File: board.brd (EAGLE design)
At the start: 26.3 x 33.6 mm, 46 parts, among them IC1 ATMEGA48/88/168-AU, IC2 TP4056, IC3 MAX31865, Q1 PH2925U, Q2 IRLML2244, U1 LM3480-3.3

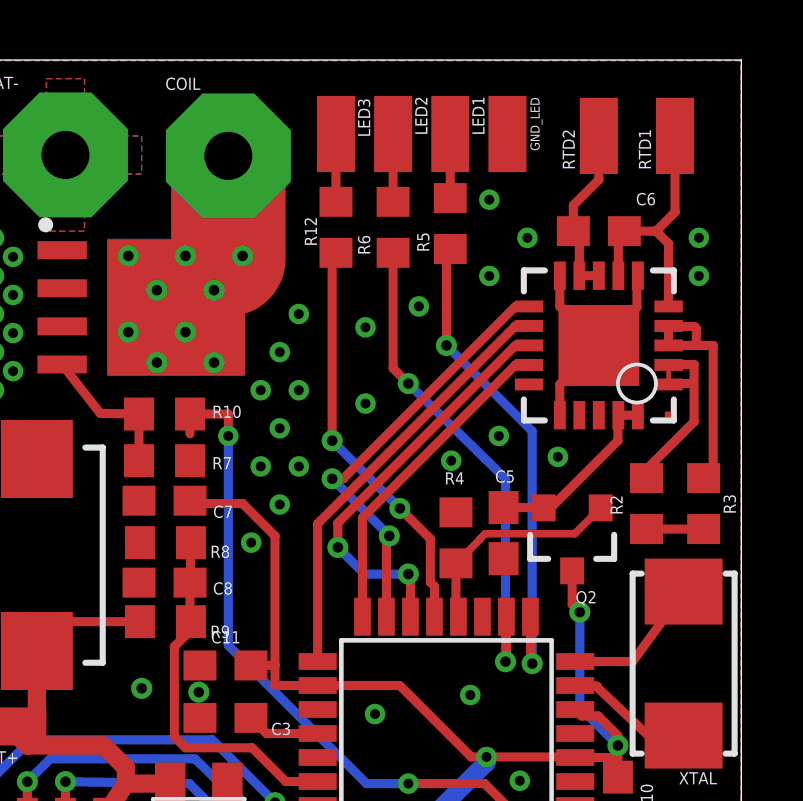
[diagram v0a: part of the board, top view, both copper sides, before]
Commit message: adding tstop for charger heat transfer
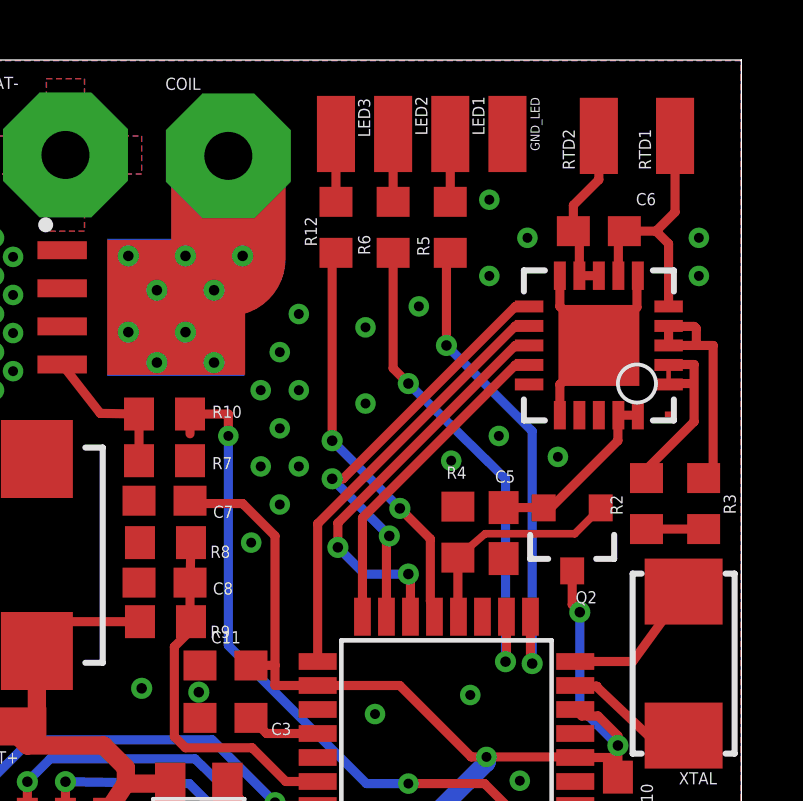
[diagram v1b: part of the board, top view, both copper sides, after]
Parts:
- moved R4 0.20 mm to (16.9, 17.9)
- moved R5 0.13 mm to (16.6, 28.1)
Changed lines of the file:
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@@
 <text x="25.4" y="0.635" size="1.6764" layer="22" rot="MR0">Vapoduino_v0.2</text>
 <rectangle x1="5.207" y1="23.114" x2="9.779" y2="27.686" layer="16"/>
+<rectangle x1="1.4605" y1="4.445" x2="4.8895" y2="6.858" layer="29"/>
 </plain>
 <attributes>
@@
 <attribute name="VALUE" x="23.1775" y="19.4945" size="1.27" layer="27" rot="R270"/>
 </element>
-<element name="R5" library="rcl" package="R0603" value="1K" x="16.637" y="28.194" smashed="yes" rot="R270">
-<attribute name="NAME" x="15.9385" y="27.2415" size="0.4064" layer="25" rot="R90"/>
-<attribute name="VALUE" x="14.732" y="28.829" size="1.27" layer="27" rot="R270"/>
+<element name="R5" library="rcl" package="R0603" value="1K" x="16.637" y="28.067" smashed="yes" rot="R270">
+<attribute name="NAME" x="15.9385" y="27.1145" size="0.4064" layer="25" rot="R90"/>
+<attribute name="VALUE" x="14.732" y="28.702" size="1.27" layer="27" rot="R270"/>
 </element>
 <element name="R6" library="rcl" package="R0603" value="1K" x="14.732" y="28.067" smashed="yes" rot="R270">
@@
 <attribute name="VALUE" x="21.717" y="17.907" size="0.4064" layer="27" rot="R180"/>
 </element>
-<element name="R4" library="rcl" package="R0603" value="10k" x="16.8275" y="17.7165" smashed="yes" rot="R90">
-<attribute name="NAME" x="16.4465" y="19.4945" size="0.4064" layer="25"/>
-<attribute name="VALUE" x="18.7325" y="17.0815" size="1.27" layer="27" rot="R90"/>
+<element name="R4" library="rcl" package="R0603" value="10k" x="16.891" y="17.907" smashed="yes" rot="R90">
+<attribute name="NAME" x="16.51" y="19.685" size="0.4064" layer="25"/>
+<attribute name="VALUE" x="18.796" y="17.272" size="1.27" layer="27" rot="R90"/>
 </element>
 <element name="R10" library="rcl" package="R0603" value="100" x="7.112" y="21.844" smashed="yes">
@@
 <contactref element="Q2" pad="1"/>
 <contactref element="R4" pad="1"/>
-<wire x1="16.91" y1="15.0876" x2="16.8275" y2="15.0876" width="0.3048" layer="1"/>
-<wire x1="16.8275" y1="15.0876" x2="16.8275" y2="16.8665" width="0.3048" layer="1"/>
-<wire x1="16.8275" y1="16.8665" x2="17.6356" y2="17.6746" width="0.254" layer="1"/>
-<wire x1="17.6356" y1="17.6746" x2="17.6356" y2="17.69098125" width="0.254" layer="1"/>
+<wire x1="16.91" y1="15.0876" x2="16.891" y2="15.0876" width="0.3048" layer="1"/>
+<wire x1="16.891" y1="15.0876" x2="16.891" y2="17.057" width="0.3048" layer="1"/>
 <wire x1="20.78915" y1="17.85465" x2="21.651" y2="18.7165" width="0.254" layer="1"/>
 <wire x1="17.79926875" y1="17.85465" x2="20.78915" y2="17.85465" width="0.254" layer="1"/>
-<wire x1="17.6356" y1="17.69098125" x2="17.79926875" y2="17.85465" width="0.254" layer="1"/>
+<wire x1="16.8736" y1="17.05598125" x2="17.79926875" y2="17.85465" width="0.254" layer="1"/>
+<wire x1="16.891" y1="17.057" x2="16.8736" y2="17.05598125" width="0" layer="19" extent="1-1"/>
 </signal>
 <signal name="D9_LED3">
 <contactref element="IC1" pad="13"/>
 <contactref element="R12" pad="2"/>
-<wire x1="16.11" y1="15.0876" x2="16.11" y2="16.10295" width="0.3048" layer="1"/>
-<wire x1="16.11" y1="16.10295" x2="15.9727" y2="16.24025" width="0.3048" layer="1"/>
-<wire x1="15.9727" y1="16.24025" x2="15.9727" y2="17.6823" width="0.3048" layer="1"/>
+<wire x1="16.11" y1="15.0876" x2="15.983" y2="15.59495" width="0.3048" layer="1"/>
+<wire x1="15.983" y1="15.59495" x2="15.9727" y2="15.60525" width="0.3048" layer="1"/>
+<wire x1="15.9727" y1="15.60525" x2="15.9727" y2="17.6823" width="0.3048" layer="1"/>
 <via x="14.95696875" y="18.69803125" extent="1-16" drill="0.35"/>
 <wire x1="14.95696875" y1="18.69803125" x2="12.7" y2="20.955" width="0.3048" layer="16"/>
@@
 <via x="16.51" y="24.13" extent="1-16" drill="0.35"/>
 <wire x1="16.51" y1="24.13" x2="16.51" y2="27.217" width="0.3048" layer="1"/>
-<wire x1="16.51" y1="27.217" x2="16.637" y2="27.344" width="0.3048" layer="1"/>
+<wire x1="16.51" y1="27.217" x2="16.637" y2="27.217" width="0.3048" layer="1"/>
 </signal>
 <signal name="VBAT">
@@
 <contactref element="R5" pad="1"/>
 <contactref element="LED1" pad="1"/>
-<wire x1="16.637" y1="31.1785" x2="16.637" y2="29.044" width="0.3048" layer="1"/>
+<wire x1="16.637" y1="31.1785" x2="16.637" y2="28.917" width="0.3048" layer="1"/>
 </signal>
 <signal name="COIL">

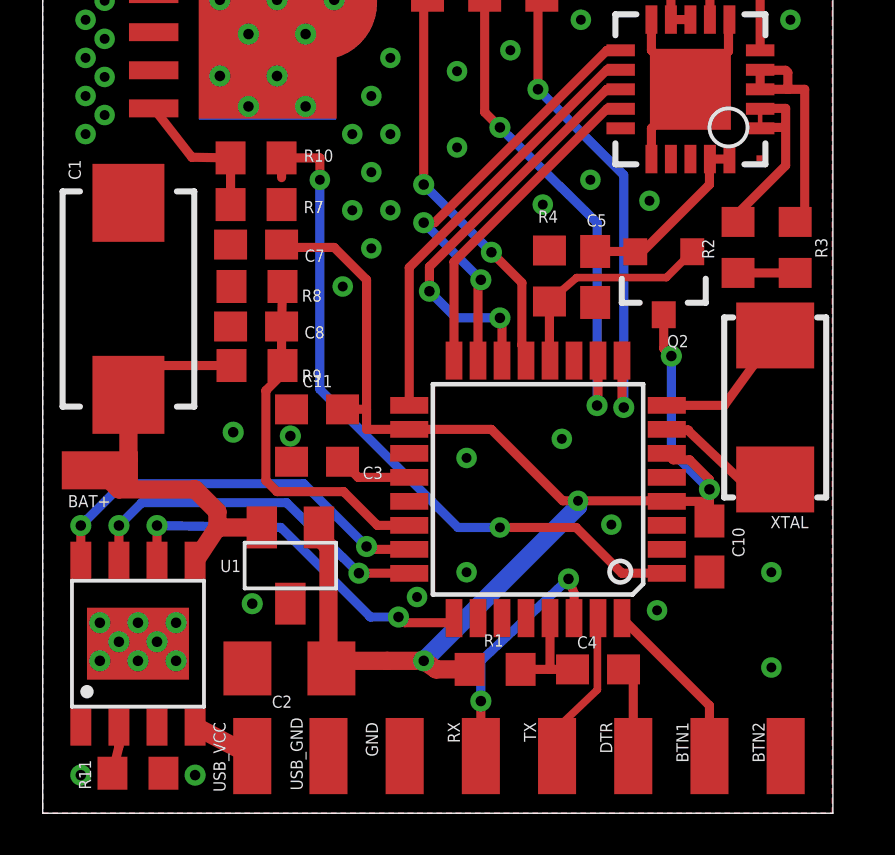
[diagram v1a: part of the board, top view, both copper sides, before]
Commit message: using MCP1703 as vreg
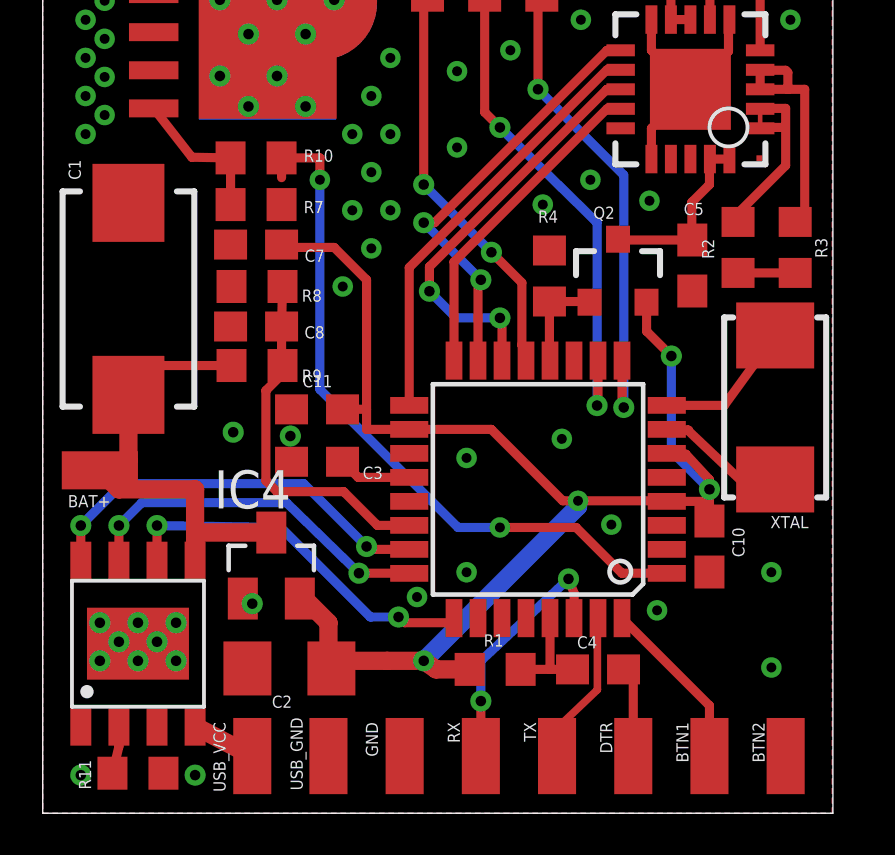
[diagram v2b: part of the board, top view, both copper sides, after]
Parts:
- removed U1: LM3480-3.3, regulators:SOT-23-3
- added IC4: MCP1703CB, linear:SOT23
- moved C5 3.26 mm to (21.7, 18.3)
- moved Q2 1.56 mm to (19.2, 18.0), turned to 0 degrees
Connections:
- net GND: now also IC4.1; no longer U1.3
- net VBAT: now also IC4.3; no longer U1.2
- net VCC: now also IC4.2, Q2.2; no longer Q2.3, U1.1
- net VCC_MAX: now also Q2.3; no longer Q2.2
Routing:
- net D8_VCC_MAX: track 7.42 -> 3.33 mm
- net VCC: track 48.8 -> 47.5 mm
- net VBAT: track 14.9 -> 15.4 mm
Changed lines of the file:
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@@
 <attribute name="VALUE" x="19.78025" y="7.33425" size="1.27" layer="27" rot="R180"/>
 </element>
-<element name="C5" library="rcl" package="C0603" value="100n" x="18.415" y="17.87525" smashed="yes" rot="R270">
-<attribute name="NAME" x="18.12925" y="19.558" size="0.4064" layer="25"/>
-<attribute name="VALUE" x="15.875" y="19.14525" size="1.27" layer="27" rot="R270"/>
+<element name="C5" library="rcl" package="C0603" value="100n" x="21.6535" y="18.25625" smashed="yes" rot="R270">
+<attribute name="NAME" x="21.36775" y="19.939" size="0.4064" layer="25"/>
+<attribute name="VALUE" x="19.1135" y="19.52625" size="1.27" layer="27" rot="R270"/>
 </element>
 <element name="C6" library="rcl" package="C0603" value="100n" x="21.59" y="27.94" smashed="yes" rot="R180">
@@
 <attribute name="VALUE" x="8.509" y="11.557" size="1.27" layer="27"/>
 </element>
-<element name="Q2" library="SparkFun-DiscreteSemi" package="SOT23-3" value="IRLML2244" x="20.701" y="17.7165" smashed="yes" rot="R180">
-<attribute name="NAME" x="21.5265" y="15.9385" size="0.4064" layer="25" rot="R180"/>
-<attribute name="PROD_ID" value="TRANS-11153" x="20.701" y="17.7165" size="1.778" layer="27" rot="R180" display="off"/>
-<attribute name="VALUE" x="21.717" y="17.907" size="0.4064" layer="27" rot="R180"/>
+<element name="Q2" library="SparkFun-DiscreteSemi" package="SOT23-3" value="IRLML2244" x="19.177" y="18.034" smashed="yes">
+<attribute name="NAME" x="18.3515" y="19.812" size="0.4064" layer="25"/>
+<attribute name="PROD_ID" value="TRANS-11153" x="19.177" y="18.034" size="1.778" layer="27" display="off"/>
+<attribute name="VALUE" x="18.161" y="17.8435" size="0.4064" layer="27"/>
 </element>
 <element name="R4" library="rcl" package="R0603" value="10k" x="16.891" y="17.907" smashed="yes" rot="R90">
@@
 <attribute name="VALUE" x="12.827" y="31.1785" size="0.0254" layer="27"/>
 </element>
-<element name="U1" library="regulators" package="SOT-23-3" value="LM3480-3.3" x="8.255" y="8.255" smashed="yes" rot="R180">
-<attribute name="NAME" x="6.604" y="8.4455" size="0.4064" layer="21" ratio="12" rot="R180"/>
-</element>
+<element name="IC4" library="linear" library_urn="urn:adsk.eagle:library:262" package="SOT23" value="MCP1703CB" x="7.62" y="8.255"/>
 </elements>
 <signals>
@@
 <wire x1="22.225" y1="10.16" x2="22.225" y2="9.74" width="0.3048" layer="1"/>
 <wire x1="12.2174" y1="12.795" x2="14.9535125" y2="12.795" width="0.3048" layer="1"/>
-<contactref element="Q2" pad="3"/>
 <wire x1="20.7836" y1="10.414" x2="17.8435" y2="10.414" width="0.3048" layer="1"/>
 <wire x1="20.7836" y1="10.414" x2="20.8026" y2="10.395" width="0.3048" layer="1"/>
-<contactref element="U1" pad="1"/>
 <wire x1="9.62325" y1="4.826" x2="10.00425" y2="5.08" width="0.6096" layer="1"/>
 <wire x1="11.481821875" y1="5.08" x2="12.7" y2="5.08" width="0.6096" layer="1"/>
@@
 <wire x1="12.7" y1="5.08" x2="17.8435" y2="10.2235" width="0.6096" layer="16"/>
 <wire x1="17.8435" y1="10.2235" x2="17.8435" y2="10.414" width="0.6096" layer="16"/>
-<wire x1="9.2075" y1="9.525" x2="9.2075" y2="9.2075" width="0.6096" layer="1"/>
-<wire x1="9.2075" y1="9.2075" x2="9.525" y2="8.89" width="0.6096" layer="1"/>
-<wire x1="9.525" y1="8.89" x2="9.525" y2="4.92425" width="0.6096" layer="1"/>
+<wire x1="8.5725" y1="7.3025" x2="9.525" y2="6.35" width="0.6096" layer="1"/>
+<wire x1="9.525" y1="6.35" x2="9.525" y2="4.92425" width="0.6096" layer="1"/>
 <wire x1="9.525" y1="4.92425" x2="9.62325" y2="4.826" width="0.6096" layer="1"/>
 <wire x1="11.43725" y1="5.035428125" x2="11.481821875" y2="5.08" width="0.3048" layer="1"/>
 <wire x1="12.7" y1="5.08" x2="13.11275" y2="4.79425" width="0.6096" layer="1"/>
 <wire x1="13.11275" y1="4.79425" x2="14.23125" y2="4.79425" width="0.6096" layer="1"/>
-<wire x1="21.56385" y1="11.7792" x2="21.0184" y2="11.7792" width="0.3048" layer="1"/>
-<wire x1="21.0184" y1="11.7792" x2="20.8026" y2="11.995" width="0.3048" layer="1"/>
+<wire x1="21.43685" y1="11.9697" x2="20.8914" y2="11.9697" width="0.3048" layer="1"/>
+<wire x1="20.8914" y1="11.9697" x2="20.8026" y2="11.995" width="0.3048" layer="1"/>
 <wire x1="22.225" y1="9.74" x2="22.225" y2="10.795" width="0.3048" layer="1"/>
 <wire x1="22.225" y1="10.795" x2="22.225" y2="11.11805" width="0.3048" layer="1"/>
-<wire x1="22.225" y1="11.11805" x2="21.56385" y2="11.7792" width="0.3048" layer="1"/>
+<wire x1="22.225" y1="11.11805" x2="21.43685" y2="11.9697" width="0.3048" layer="1"/>
 <wire x1="17.8435" y1="10.414" x2="17.3345125" y2="10.414" width="0.3048" layer="1"/>
 <wire x1="17.3345125" y1="10.414" x2="14.9535125" y2="12.795" width="0.3048" layer="1"/>
@@
 <wire x1="22.225" y1="10.795" x2="20.955" y2="12.065" width="0.3048" layer="16"/>
 <wire x1="20.955" y1="12.065" x2="20.955" y2="15.24" width="0.3048" layer="16"/>
-<wire x1="20.701" y1="16.6165" x2="20.701" y2="15.494" width="0.3048" layer="1"/>
-<wire x1="20.701" y1="15.494" x2="20.955" y2="15.24" width="0.3048" layer="1"/>
+<wire x1="20.1295" y1="16.9545" x2="20.1295" y2="16.0655" width="0.3048" layer="1"/>
+<wire x1="20.1295" y1="16.0655" x2="20.955" y2="15.24" width="0.3048" layer="1"/>
 <via x="20.955" y="15.24" extent="1-16" drill="0.35"/>
 <wire x1="9.994" y1="13.462" x2="9.994" y2="13.466090625" width="0.3048" layer="1"/>
@@
 <wire x1="10.795" y1="13.466090625" x2="10.795" y2="12.795" width="0.3048" layer="1"/>
 <wire x1="10.795" y1="12.795" x2="12.2174" y2="12.795" width="0.3048" layer="1"/>
+<contactref element="Q2" pad="2"/>
+<contactref element="IC4" pad="2"/>
+<wire x1="20.1295" y1="16.9545" x2="20.127" y2="17.034" width="0" layer="19" extent="1-1"/>
+<wire x1="8.57" y1="7.155" x2="8.5725" y2="7.3025" width="0" layer="19" extent="1-1"/>
 </signal>
 <signal name="GND">
@@
 <vertex x="3.175" y="31.115"/>
 </polygon>
-<contactref element="U1" pad="3"/>
 <via x="8.255" y="12.573" extent="1-16" drill="0.35"/>
 <via x="6.985" y="6.985" extent="1-16" drill="0.35"/>
@@
 <via x="16.66875" y="20.28825" extent="1-16" drill="0.3302"/>
 <via x="20.22475" y="20.41525" extent="1-16" drill="0.3302"/>
+<contactref element="IC4" pad="1"/>
 </signal>
 <signal name="RXI">
@@
 <wire x1="16.91" y1="15.0876" x2="16.891" y2="15.0876" width="0.3048" layer="1"/>
 <wire x1="16.891" y1="15.0876" x2="16.891" y2="17.057" width="0.3048" layer="1"/>
-<wire x1="20.78915" y1="17.85465" x2="21.651" y2="18.7165" width="0.254" layer="1"/>
-<wire x1="17.79926875" y1="17.85465" x2="20.78915" y2="17.85465" width="0.254" layer="1"/>
-<wire x1="16.8736" y1="17.05598125" x2="17.79926875" y2="17.85465" width="0.254" layer="1"/>
-<wire x1="16.891" y1="17.057" x2="16.8736" y2="17.05598125" width="0" layer="19" extent="1-1"/>
+<wire x1="16.891" y1="17.057" x2="18.204" y2="17.057" width="0.3048" layer="1"/>
+<wire x1="18.204" y1="17.057" x2="18.227" y2="17.034" width="0.3048" layer="1"/>
 </signal>
 <signal name="D9_LED3">
@@
 <contactref element="C1" pad="+"/>
 <contactref element="BAT+" pad="1"/>
-<contactref element="U1" pad="2"/>
 <wire x1="2.8575" y1="11.7475" x2="2.8575" y2="13.945" width="0.6096" layer="1"/>
 <wire x1="2.8575" y1="11.7475" x2="1.905" y2="11.43" width="0.6096" layer="1"/>
 <wire x1="1.905" y1="11.43" x2="2.54" y2="10.795" width="0.6096" layer="1"/>
 <wire x1="2.54" y1="10.795" x2="5.08" y2="10.795" width="0.6096" layer="1"/>
-<wire x1="5.8225" y1="9.525" x2="5.08" y2="8.4015" width="0.6096" layer="1"/>
-<wire x1="5.8225" y1="9.525" x2="7.3025" y2="9.525" width="0.6096" layer="1"/>
-<wire x1="5.08" y1="10.795" x2="5.8225" y2="10.0525" width="0.6096" layer="1"/>
-<wire x1="5.8225" y1="10.0525" x2="5.8225" y2="9.525" width="0.6096" layer="1"/>
 <wire x1="2.8575" y1="13.945" x2="3.835" y2="14.9225" width="0.3048" layer="1"/>
 <wire x1="3.835" y1="14.9225" x2="6.29375" y2="14.9225" width="0.3048" layer="1"/>
+<contactref element="IC4" pad="3"/>
+<wire x1="5.08" y1="9.37239375" x2="5.08" y2="10.795" width="0.6096" layer="1"/>
+<wire x1="5.08" y1="9.37239375" x2="5.08" y2="8.4015" width="0.6096" layer="1"/>
+<wire x1="7.62" y1="9.355" x2="5.09739375" y2="9.355" width="0.6096" layer="1"/>
+<wire x1="5.09739375" y1="9.355" x2="5.08" y2="9.37239375" width="0.6096" layer="1"/>
 </signal>
 <signal name="VUSB">
@@
 <contactref element="IC3" pad="20"/>
 <contactref element="C5" pad="1"/>
-<contactref element="Q2" pad="2"/>
 <wire x1="22.24" y1="21.805" x2="22.89" y2="21.805" width="0.3048" layer="1"/>
-<wire x1="18.415" y1="18.72525" x2="19.74225" y2="18.72525" width="0.3048" layer="1"/>
-<wire x1="19.74225" y1="18.72525" x2="19.751" y2="18.7165" width="0.3048" layer="1"/>
-<wire x1="19.751" y1="18.7165" x2="19.9865" y2="18.7165" width="0.3048" layer="1"/>
-<wire x1="19.9865" y1="18.7165" x2="22.225" y2="20.955" width="0.3048" layer="1"/>
+<wire x1="21.6535" y1="19.10625" x2="19.17075" y2="19.10625" width="0.3048" layer="1"/>
+<wire x1="21.6375" y1="19.0975" x2="21.6375" y2="20.3675" width="0.3048" layer="1"/>
+<wire x1="21.6375" y1="20.3675" x2="22.225" y2="20.955" width="0.3048" layer="1"/>
 <wire x1="22.225" y1="20.955" x2="22.225" y2="21.79" width="0.3048" layer="1"/>
 <wire x1="22.225" y1="21.79" x2="22.24" y2="21.805" width="0.3048" layer="1"/>
+<contactref element="Q2" pad="3"/>
+<wire x1="21.6535" y1="19.10625" x2="21.6375" y2="19.0975" width="0" layer="19" extent="1-1"/>
+<wire x1="19.177" y1="19.134" x2="19.17075" y2="19.10625" width="0" layer="19" extent="1-1"/>
 </signal>
 <signal name="GATE">
@@
 </board>
 </drawing>
+<compatibility>
+<note version="8.2" severity="warning">
+Since Version 8.2, Eagle supports online libraries. The ids
+of those online libraries will not be understood (or retained)
+with this version.
+</note>
+</compatibility>
 </eagle>
